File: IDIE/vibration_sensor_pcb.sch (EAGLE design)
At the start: 3 parts, among them IC1 LORA-E5, IC2 STM32L071KBT6

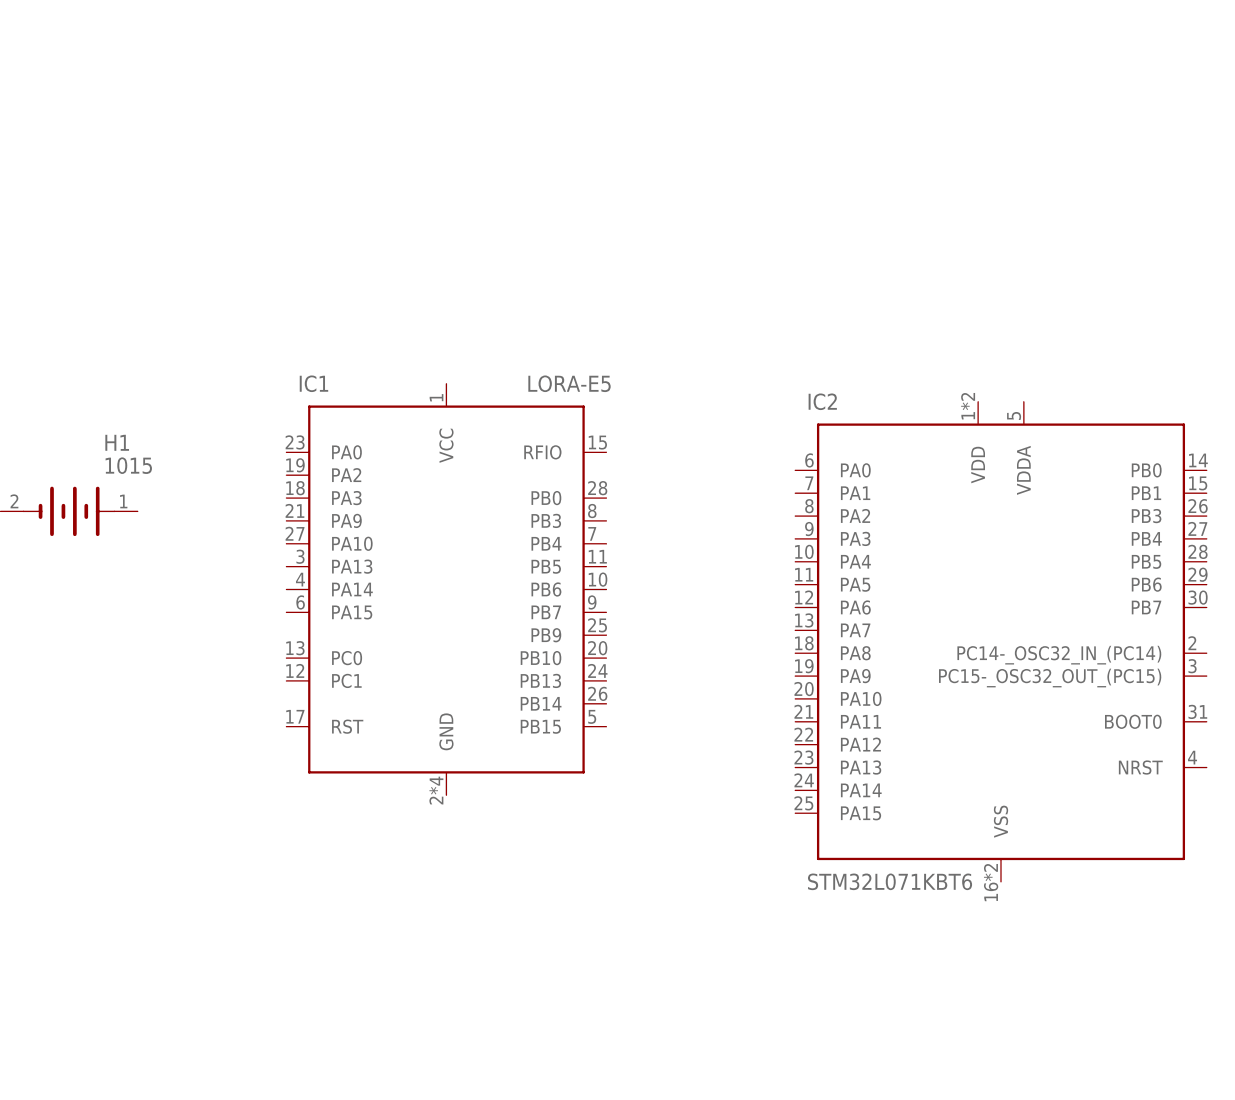
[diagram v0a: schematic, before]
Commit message: add and update pcb design with lora, stm, battery
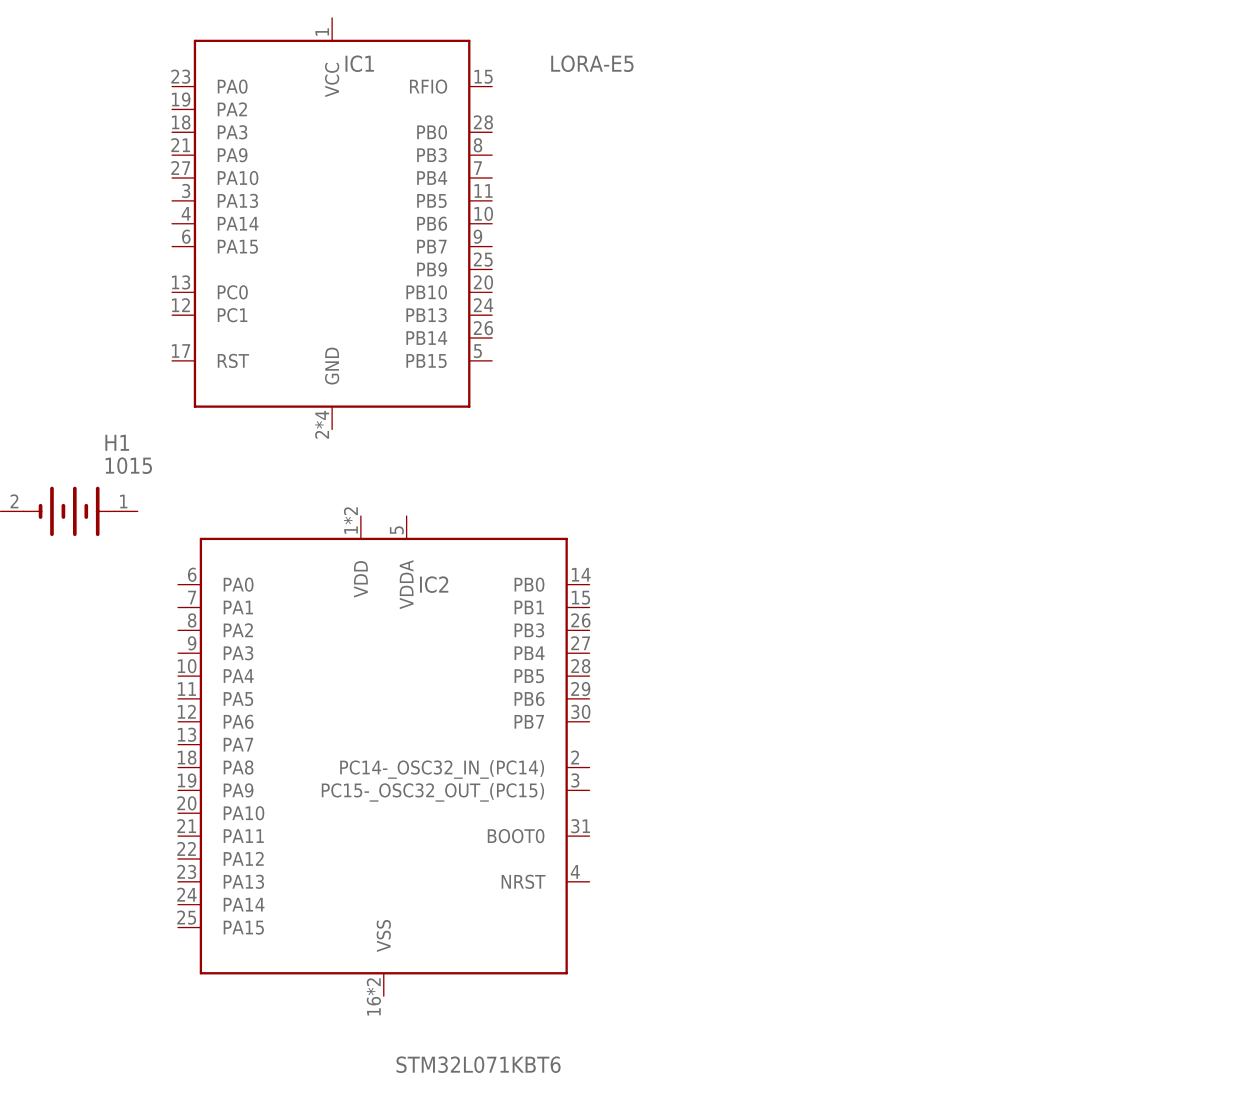
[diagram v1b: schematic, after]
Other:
- moved on the sheet: IC1, IC2
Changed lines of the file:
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@@
 <setting verticaltext="up"/>
 </settings>
-<grid distance="1" unitdist="mm" unit="mm" style="lines" multiple="1" display="no" altdistance="1" altunitdist="mm" altunit="mm"/>
+<grid distance="0.1" unitdist="inch" unit="inch" style="lines" multiple="1" display="no" altdistance="0.01" altunitdist="inch" altunit="inch"/>
 <layers>
 <layer number="1" name="Top" color="4" fill="1" visible="no" active="no"/>
@@
 </classes>
 <parts>
-<part name="FRAME1" library="frames" library_urn="urn:adsk.eagle:library:229" deviceset="A5L-LOC" device=""/>
 <part name="H1" library="SamacSys_Parts" deviceset="1015" device=""/>
 <part name="IC1" library="SamacSys_Parts" deviceset="LORA-E5" device=""/>
 <part name="IC2" library="SamacSys_Parts" deviceset="STM32L071KBT6" device=""/>
+<part name="FRAME1" library="frames" library_urn="urn:adsk.eagle:library:229" deviceset="A4L-LOC" device=""/>
 </parts>
 <sheets>
@@
 </plain>
 <instances>
-<instance part="FRAME1" gate="G$1" x="0" y="0" smashed="yes">
-<attribute name="DRAWING_NAME" x="140.97" y="15.24" size="2.54" layer="94"/>
-<attribute name="LAST_DATE_TIME" x="140.97" y="10.16" size="2.286" layer="94"/>
-<attribute name="SHEET" x="154.305" y="5.08" size="2.54" layer="94"/>
-</instance>
 <instance part="H1" gate="G$1" x="22.86" y="99.06" smashed="yes">
 <attribute name="NAME" x="26.67" y="106.68" size="1.778" layer="95" align="center-left"/>
 <attribute name="VALUE" x="26.67" y="104.14" size="1.778" layer="96" align="center-left"/>
 </instance>
-<instance part="IC1" gate="G$1" x="47" y="98" smashed="yes">
-<attribute name="NAME" x="48.27" y="113.24" size="1.778" layer="95" align="center-left"/>
-<attribute name="VALUE" x="73.67" y="113.24" size="1.778" layer="96" align="center-left"/>
+<instance part="IC1" gate="G$1" x="52.08" y="133.56" smashed="yes">
+<attribute name="NAME" x="53.35" y="148.8" size="1.778" layer="95" align="center-left"/>
+<attribute name="VALUE" x="76.21" y="148.8" size="1.778" layer="96" align="center-left"/>
 </instance>
-<instance part="IC2" gate="G$1" x="101" y="96" smashed="yes">
-<attribute name="NAME" x="104.81" y="111.24" size="1.778" layer="95" align="center-left"/>
-<attribute name="VALUE" x="104.81" y="57.9" size="1.778" layer="96" align="center-left"/>
+<instance part="IC2" gate="G$1" x="57.82" y="75.68" smashed="yes">
+<attribute name="NAME" x="61.63" y="90.92" size="1.778" layer="95" align="center-left"/>
+<attribute name="VALUE" x="59.09" y="37.58" size="1.778" layer="96" align="center-left"/>
+</instance>
+<instance part="FRAME1" gate="G$1" x="0" y="0" smashed="yes">
+<attribute name="DRAWING_NAME" x="217.17" y="15.24" size="2.54" layer="94"/>
+<attribute name="LAST_DATE_TIME" x="217.17" y="10.16" size="2.286" layer="94"/>
+<attribute name="SHEET" x="230.505" y="5.08" size="2.54" layer="94"/>
 </instance>
 </instances>

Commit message: add new design with other modules
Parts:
- added ANT1: ANTENNA, SamacSys_Parts:ANTENNA
- added IC3: FXLS8974CFR3, SamacSys_Parts:FXLS8974CFR3
- added IC4: FXLS8971CFR1, SamacSys_Parts:FXLS8971CFR1
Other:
- moved on the sheet: H1, IC1, IC2
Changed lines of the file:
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@@
 <part name="IC2" library="SamacSys_Parts" deviceset="STM32L071KBT6" device=""/>
 <part name="FRAME1" library="frames" library_urn="urn:adsk.eagle:library:229" deviceset="A4L-LOC" device=""/>
+<part name="IC3" library="SamacSys_Parts" deviceset="FXLS8974CFR3" device=""/>
+<part name="IC4" library="SamacSys_Parts" deviceset="FXLS8971CFR1" device=""/>
+<part name="ANT1" library="SamacSys_Parts" deviceset="ANTENNA" device=""/>
 </parts>
 <sheets>
@@
 </plain>
 <instances>
-<instance part="H1" gate="G$1" x="22.86" y="99.06" smashed="yes">
-<attribute name="NAME" x="26.67" y="106.68" size="1.778" layer="95" align="center-left"/>
-<attribute name="VALUE" x="26.67" y="104.14" size="1.778" layer="96" align="center-left"/>
+<instance part="H1" gate="G$1" x="96.52" y="127" smashed="yes">
+<attribute name="NAME" x="100.33" y="134.62" size="1.778" layer="95" align="center-left"/>
+<attribute name="VALUE" x="100.33" y="132.08" size="1.778" layer="96" align="center-left"/>
 </instance>
-<instance part="IC1" gate="G$1" x="52.08" y="133.56" smashed="yes">
-<attribute name="NAME" x="53.35" y="148.8" size="1.778" layer="95" align="center-left"/>
-<attribute name="VALUE" x="76.21" y="148.8" size="1.778" layer="96" align="center-left"/>
+<instance part="IC1" gate="G$1" x="189.24" y="133.56" smashed="yes">
+<attribute name="NAME" x="175.27" y="153.88" size="1.778" layer="95" align="center-left"/>
+<attribute name="VALUE" x="193.05" y="153.88" size="1.778" layer="96" align="center-left"/>
 </instance>
-<instance part="IC2" gate="G$1" x="57.82" y="75.68" smashed="yes">
-<attribute name="NAME" x="61.63" y="90.92" size="1.778" layer="95" align="center-left"/>
-<attribute name="VALUE" x="59.09" y="37.58" size="1.778" layer="96" align="center-left"/>
+<instance part="IC2" gate="G$1" x="98.46" y="83.3" smashed="yes">
+<attribute name="NAME" x="79.41" y="106.16" size="1.778" layer="95" align="center-left"/>
+<attribute name="VALUE" x="74.33" y="52.82" size="1.778" layer="96" align="center-left"/>
 </instance>
 <instance part="FRAME1" gate="G$1" x="0" y="0" smashed="yes">
@@
 <attribute name="SHEET" x="230.505" y="5.08" size="2.54" layer="94"/>
 </instance>
+<instance part="IC3" gate="G$1" x="190.5" y="78.74" smashed="yes">
+<attribute name="NAME" x="173.99" y="88.9" size="1.778" layer="95" align="center-left"/>
+<attribute name="VALUE" x="173.99" y="68.58" size="1.778" layer="96" align="center-left"/>
+</instance>
+<instance part="IC4" gate="G$1" x="190.5" y="53.34" smashed="yes">
+<attribute name="NAME" x="173.99" y="63.5" size="1.778" layer="95" align="center-left"/>
+<attribute name="VALUE" x="173.99" y="43.18" size="1.778" layer="96" align="center-left"/>
+</instance>
+<instance part="ANT1" gate="G$1" x="139.7" y="129.54" smashed="yes">
+<attribute name="NAME" x="138.43" y="139.7" size="1.778" layer="95" align="center-left"/>
+<attribute name="VALUE" x="138.43" y="137.16" size="1.778" layer="96" align="center-left"/>
+</instance>
 </instances>

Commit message: UPLOADING todo el diseño nuevo de pcb con conexiones de spi e i2c
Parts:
- added C1, C2: DNP, rcl:C-EUC0603
- added C3: 4.7uF, rcl:C-EUC0603
- added C4, C5, C7: 0.1uF, rcl:C-EUC0603
- added C6: 1uF, rcl:C-EUC0603
- added JMP1, JMP2, JMP3: 0R-JUMPA, jump-0r-smd:0R-JUMPA
- added Q1: SI2305B-TP, SamacSys_Parts:SI2305B-TP
- added R1: 0, rcl:R-US_R0603
- added R2, R5, R6: 100k, rcl:R-US_R0603
- added R3, R4: 22, rcl:R-US_R0603
- added R7: DNP, rcl:R-US_R0603
- added T1: (no value), transistor-neu-to92:MUN2211T1-NPN_DRIVER-SC59-BEC
- added TP1, TP2, TP3, TP4, TP5: PTR1TP11R, testpad:PTR1TP11R
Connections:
- new net +3V3: C3.1, C4.1, C6.1, C7.1, IC1.VCC, IC2.VDD, IC2.VDDA, IC3.VDD, IC4.VDD, JMP3-0R.3, R2.2, R5.2, R6.2
- new net ANT: ANT1.FEED, C2.1, R1.2
- new net BOOT: IC1.PB13, TP3.TP
- new net E5_RST: C5.1, IC1.RST, R2.1, T1.C
- new net GND: C1.2, C2.2, C3.2, C4.2, C5.2, C6.2, C7.2, H1.-, IC1.GND, IC2.VSS, IC3.BT_MODE, IC3.GND, IC4.BT_MODE, IC4.GND, JMP3-0R.1, R7.1, T1.E
- new net I2C_SCL: IC2.PA9
- new net I2C_SDA: IC2.PA10
- new net INT1: IC3.INT1/MOT_DET, IC4.INT1/MOT_DET, R6.1
- new net INT2: IC3.INT2/EXT_TRIG, IC4.INT2/EXT/TRIG, R5.1
- new net MCU_RXD: IC2.PA3, R3.2
- new net MCU_SWCLK: IC2.PA14
- new net MCU_SWDIO: IC2.PA13
- new net MCU_TXD: IC2.PA2, R4.2
- new net MD_RST: T1.B
- new net N$1: IC3.INTF_SEL, IC4.INTF_SEL, JMP3-0R.2
- new net N$3: IC1.PB6, R3.1, TP5.TP
- new net N$4: IC1.PB7, R4.1, TP4.TP
- new net PA15: IC2.PA15
- new net PA8: IC2.PA8
- new net PB3: IC2.PB3
- new net PB4: IC2.PB4
- new net PB5: IC2.PB5
- new net PB6: IC2.PB6
- new net PB7: IC2.PB7
- new net RF_IO: C1.1, IC1.RFIO, R1.1
- new net SCL: JMP2-0R.3
- new net SCL/SCLK: IC3.SCL/SCLK, IC4.SCL/SCLK, JMP2-0R.2
- new net SDA: JMP1-0R.3
- new net SDA/MOSI: IC3.SDA/SPI_MOSI, IC4.SDA/SPI_MOSI, JMP1-0R.2
- new net SPI_CS: IC2.PA4, IC3.SPI_CS_B, IC4.SPI_CSB
- new net SPI_MISO: IC2.PA6, IC3.SA0/SPI_MISO, IC4.SA0/SPI_MISO, R7.2
- new net SPI_MOSI: IC2.PA7, JMP1-0R.1
- new net SPI_SCK: IC2.PA5
- new net SPI_SCLK: JMP2-0R.1
- new net SWCLK: IC1.PA14, TP1.TP
- new net SWDIO: IC1.PA13, TP2.TP
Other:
- moved on the sheet: ANT1, H1, IC1, IC2, IC3, IC4

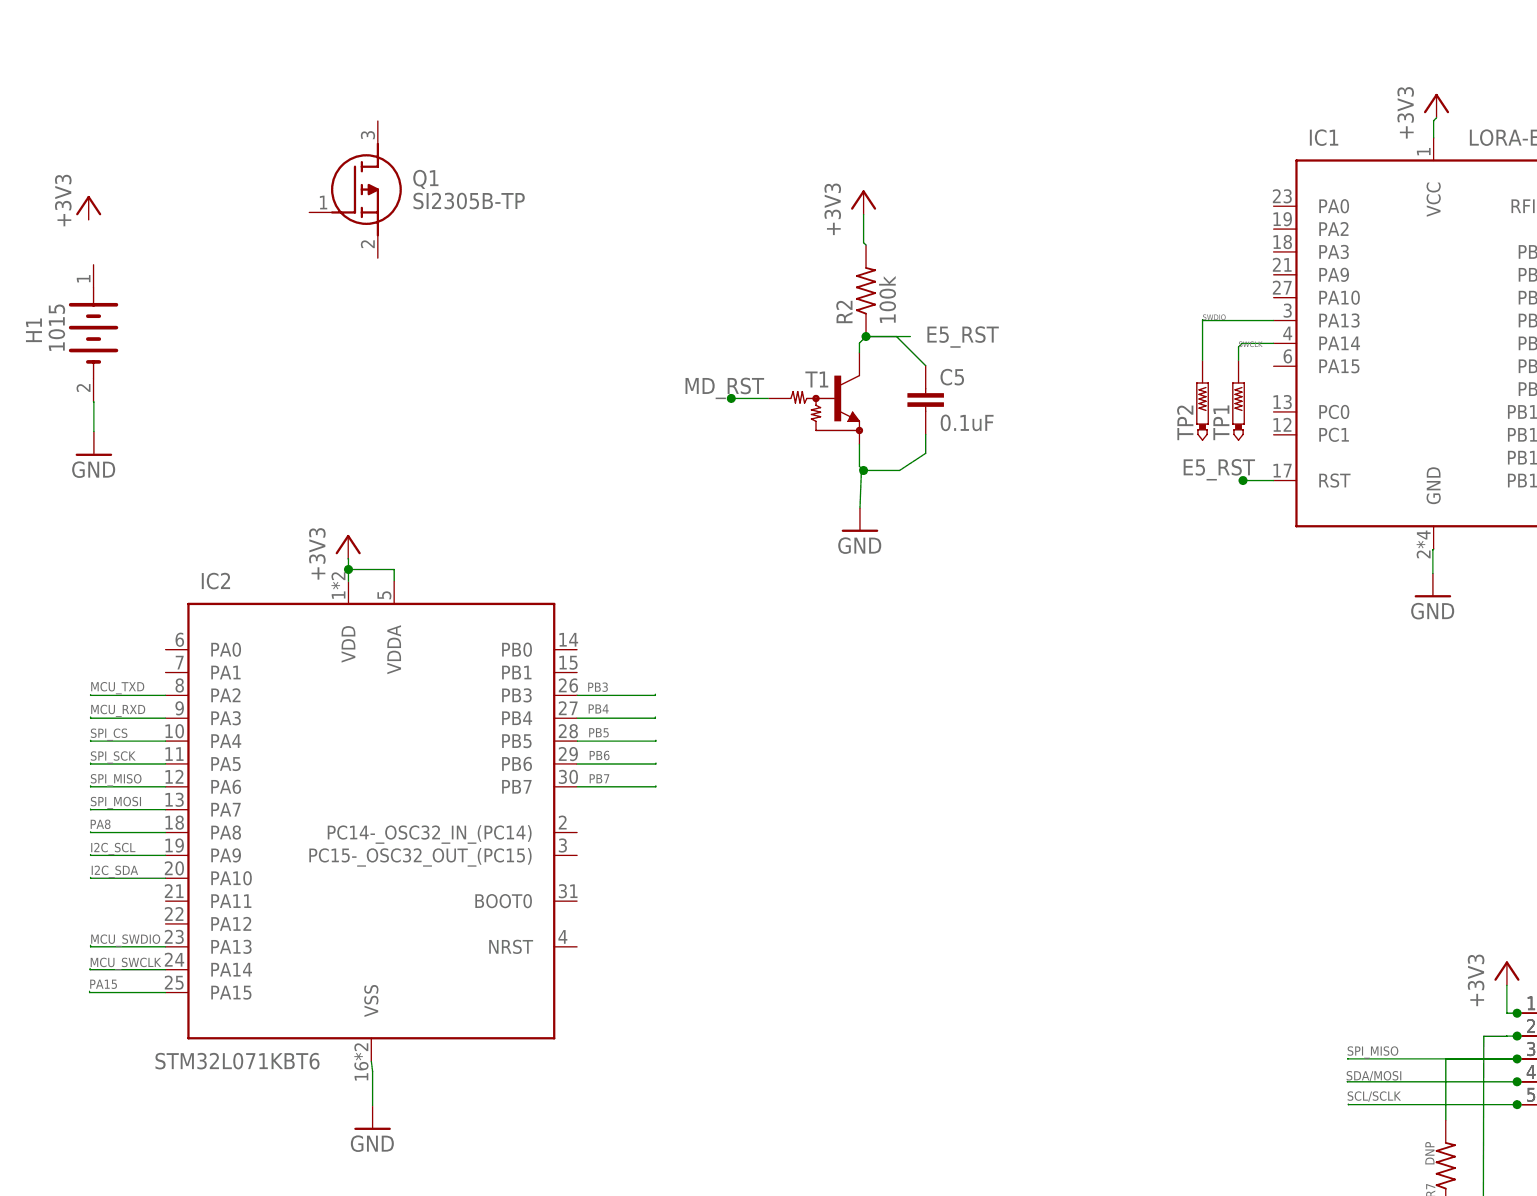
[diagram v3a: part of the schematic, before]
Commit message: ADD crista sensor hall
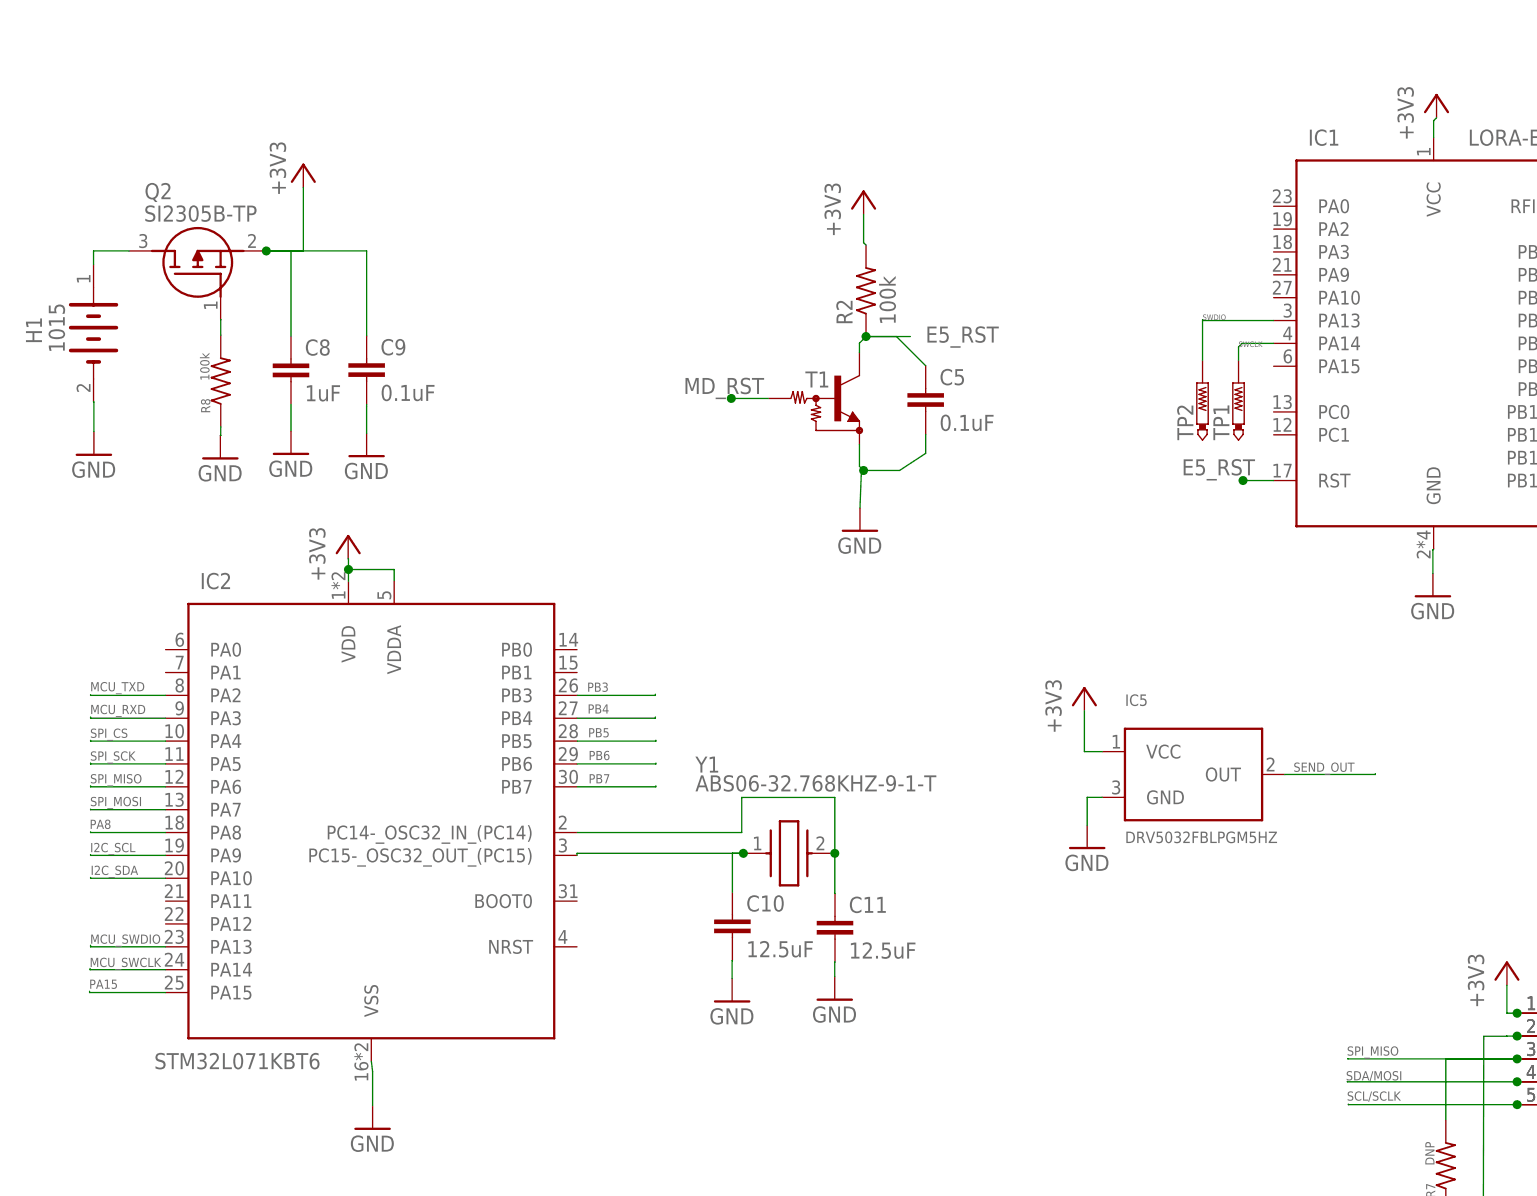
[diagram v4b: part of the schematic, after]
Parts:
- removed Q1: SI2305B-TP, SamacSys_Parts:SI2305B-TP
- added C10, C11: 12.5uF, rcl:C-EUC0603
- added C8: 1uF, rcl:C-EUC0603
- added C9: 0.1uF, rcl:C-EUC0603
- added IC5: DRV5032FBLPGM5HZ, transistor:DRV5032FBLPGM5HZ
- added Q2: SI2305B-TP, SamacSys_Parts:SI2305B-TP
- added R8: 100k, rcl:R-US_R0603
- added Y1: ABS06-32.768KHZ-9-1-T, SamacSys_Parts:ABS06-32.768KHZ-9-1-T
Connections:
- new net N$2: H1.+, Q2.D
- new net N$6: Q2.G, R8.2
- new net N$7: C11.1, IC2.PC14-_OSC32_IN_(PC14), Y1.2
- new net N$8: C10.1, IC2.PC15-_OSC32_OUT_(PC15), Y1.1
- new net SEND_OUT: IC5.OUT
- net +3V3: now also C8.1, C9.1, IC5.VCC, Q2.S
- net GND: now also C10.2, C11.2, C8.2, C9.2, IC5.GND, R8.1
